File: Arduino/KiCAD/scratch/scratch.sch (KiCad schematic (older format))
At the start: 3 parts

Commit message: Worked on basic schematic
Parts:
- added R? (x5): 220, symbol Device:R_US
- added RV? (x2): Joystick, symbol Device:R_POT_Dual_Separate
- added SW? (x4): SW_Push, symbol Switch:SW_Push
- R?: value R_US -> 220
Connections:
- net +5V: now also A?.27 (+5V), R?.2, SW?.1, SW?.1, SW?.1, SW?.1
- net B1: now also A?.13 (D10)
- net GNDREF: now also A?.29 (GND), A?.4 (GND), R?.2, R?.2, R?.2, R?.2, RV?.3, RV?.4
- net B4: now reaches A?.10 (D7)
- net B4: now also R?.1, SW?.2
- net B3: now reaches A?.11 (D8)
- net B3: now also R?.1, SW?.2
- net B2: now reaches A?.12 (D9)
- net B2: now also R?.1, SW?.2
- net A1: now reaches A?.19 (A0)
- net A1: now also RV?.5
- net A2: now reaches A?.20 (A1)
- net A2: now also RV?.2
- net JB1: now reaches A?.6 (D3)
- net JB1: now also R?.1, SW?.2
- new net: R?.1, RV?.1, RV?.6
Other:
- moved on the sheet: R?, SW?

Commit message: book keeping
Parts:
- gave numbers to parts that had none: 13
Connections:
- net A1: now also RV1.2; no longer RV1.5
- net A2: now also RV1.5; no longer RV1.2
- net GNDREF: now also RV1.1, RV1.6; no longer RV1.3, RV1.4
- new net: R3.1, RV1.3, RV1.4
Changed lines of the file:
@@
 $EndDescr
 $Comp
-L MCU_Module:Arduino_Nano_v2.x A?
+L MCU_Module:Arduino_Nano_v2.x A1
 U 1 1 5EB70971
 P 3450 2700
-F 0 "A?" H 3450 1611 50  0000 C CNN
+F 0 "A1" H 3450 1611 50  0000 C CNN
 F 1 "Arduino_Nano_v2.x" H 3450 1520 50  0000 C CNN
 F 2 "Module:Arduino_Nano" H 3450 2700 50  0001 C CIN
@@
 $EndComp
 $Comp
-L Switch:SW_Push SW?
+L Switch:SW_Push SW1
 U 1 1 5EB728D4
 P 5850 1900
-F 0 "SW?" H 5850 2185 50  0000 C CNN
+F 0 "SW1" H 5850 2185 50  0000 C CNN
 F 1 "SW_Push" H 5850 2094 50  0000 C CNN
 F 2 "" H 5850 2100 50  0001 C CNN
@@
 $EndComp
 $Comp
-L Device:R_US R?
+L Device:R_US R1
 U 1 1 5EB73329
 P 6050 2150
-F 0 "R?" H 6118 2196 50  0000 L CNN
+F 0 "R1" H 6118 2196 50  0000 L CNN
 F 1 "220" H 6118 2105 50  0000 L CNN
 F 2 "" V 6090 2140 50  0001 C CNN
@@
 $EndComp
 $Comp
-L power:GNDREF #PWR?
+L power:GNDREF #PWR04
 U 1 1 5EB73B39
 P 6050 2350
-F 0 "#PWR?" H 6050 2100 50  0001 C CNN
+F 0 "#PWR04" H 6050 2100 50  0001 C CNN
 F 1 "GNDREF" H 6055 2177 50  0000 C CNN
 F 2 "" H 6050 2350 50  0001 C CNN
@@
 $EndComp
 $Comp
-L power:+5V #PWR?
+L power:+5V #PWR03
 U 1 1 5EB7405F
 P 5550 1700
-F 0 "#PWR?" H 5550 1550 50  0001 C CNN
+F 0 "#PWR03" H 5550 1550 50  0001 C CNN
 F 1 "+5V" H 5565 1873 50  0000 C CNN
 F 2 "" H 5550 1700 50  0001 C CNN
@@
 	6050 1950 6050 2000
 $Comp
-L Switch:SW_Push SW?
+L Switch:SW_Push SW2
 U 1 1 5EB7902D
 P 6850 1900
-F 0 "SW?" H 6850 2185 50  0000 C CNN
+F 0 "SW2" H 6850 2185 50  0000 C CNN
 F 1 "SW_Push" H 6850 2094 50  0000 C CNN
 F 2 "" H 6850 2100 50  0001 C CNN
@@
 $EndComp
 $Comp
-L Device:R_US R?
+L Device:R_US R2
 U 1 1 5EB79033
 P 7050 2150
-F 0 "R?" H 7118 2196 50  0000 L CNN
+F 0 "R2" H 7118 2196 50  0000 L CNN
 F 1 "220" H 7118 2105 50  0000 L CNN
 F 2 "" V 7090 2140 50  0001 C CNN
@@
 $EndComp
 $Comp
-L power:GNDREF #PWR?
+L power:GNDREF #PWR06
 U 1 1 5EB79039
 P 7050 2350
-F 0 "#PWR?" H 7050 2100 50  0001 C CNN
+F 0 "#PWR06" H 7050 2100 50  0001 C CNN
 F 1 "GNDREF" H 7055 2177 50  0000 C CNN
 F 2 "" H 7050 2350 50  0001 C CNN
@@
 $EndComp
 $Comp
-L power:+5V #PWR?
+L power:+5V #PWR05
 U 1 1 5EB7903F
 P 6550 1700
-F 0 "#PWR?" H 6550 1550 50  0001 C CNN
+F 0 "#PWR05" H 6550 1550 50  0001 C CNN
 F 1 "+5V" H 6565 1873 50  0000 C CNN
 F 2 "" H 6550 1700 50  0001 C CNN
@@
 	7050 1950 7050 2000
 $Comp
-L Switch:SW_Push SW?
+L Switch:SW_Push SW4
 U 1 1 5EB7CE6C
 P 7850 1900
-F 0 "SW?" H 7850 2185 50  0000 C CNN
+F 0 "SW4" H 7850 2185 50  0000 C CNN
 F 1 "SW_Push" H 7850 2094 50  0000 C CNN
 F 2 "" H 7850 2100 50  0001 C CNN
@@
 $EndComp
 $Comp
-L Device:R_US R?
+L Device:R_US R5
 U 1 1 5EB7CE72
 P 8050 2150
-F 0 "R?" H 8118 2196 50  0000 L CNN
+F 0 "R5" H 8118 2196 50  0000 L CNN
 F 1 "220" H 8118 2105 50  0000 L CNN
 F 2 "" V 8090 2140 50  0001 C CNN
@@
 $EndComp
 $Comp
-L power:GNDREF #PWR?
+L power:GNDREF #PWR011
 U 1 1 5EB7CE78
 P 8050 2350
-F 0 "#PWR?" H 8050 2100 50  0001 C CNN
+F 0 "#PWR011" H 8050 2100 50  0001 C CNN
 F 1 "GNDREF" H 8055 2177 50  0000 C CNN
 F 2 "" H 8050 2350 50  0001 C CNN
@@
 $EndComp
 $Comp
-L power:+5V #PWR?
+L power:+5V #PWR09
 U 1 1 5EB7CE7E
 P 7550 1700
-F 0 "#PWR?" H 7550 1550 50  0001 C CNN
+F 0 "#PWR09" H 7550 1550 50  0001 C CNN
 F 1 "+5V" H 7565 1873 50  0000 C CNN
 F 2 "" H 7550 1700 50  0001 C CNN
@@
 	8050 1950 8050 2000
 $Comp
-L Switch:SW_Push SW?
+L Switch:SW_Push SW5
 U 1 1 5EB7E073
 P 8850 1900
-F 0 "SW?" H 8850 2185 50  0000 C CNN
+F 0 "SW5" H 8850 2185 50  0000 C CNN
 F 1 "SW_Push" H 8850 2094 50  0000 C CNN
 F 2 "" H 8850 2100 50  0001 C CNN
@@
 $EndComp
 $Comp
-L Device:R_US R?
+L Device:R_US R6
 U 1 1 5EB7E079
 P 9050 2150
-F 0 "R?" H 9118 2196 50  0000 L CNN
+F 0 "R6" H 9118 2196 50  0000 L CNN
 F 1 "220" H 9118 2105 50  0000 L CNN
 F 2 "" V 9090 2140 50  0001 C CNN
@@
 $EndComp
 $Comp
-L power:GNDREF #PWR?
+L power:GNDREF #PWR013
 U 1 1 5EB7E07F
 P 9050 2350
-F 0 "#PWR?" H 9050 2100 50  0001 C CNN
+F 0 "#PWR013" H 9050 2100 50  0001 C CNN
 F 1 "GNDREF" H 9055 2177 50  0000 C CNN
 F 2 "" H 9050 2350 50  0001 C CNN
@@
 $EndComp
 $Comp
-L power:+5V #PWR?
+L power:+5V #PWR012
 U 1 1 5EB7E085
 P 8550 1700
-F 0 "#PWR?" H 8550 1550 50  0001 C CNN
+F 0 "#PWR012" H 8550 1550 50  0001 C CNN
 F 1 "+5V" H 8565 1873 50  0000 C CNN
 F 2 "" H 8550 1700 50  0001 C CNN
@@
 	2700 2800 2950 2800
 $Comp
-L power:GNDREF #PWR?
+L power:GNDREF #PWR02
 U 1 1 5EB79925
 P 4050 3700
-F 0 "#PWR?" H 4050 3450 50  0001 C CNN
+F 0 "#PWR02" H 4050 3450 50  0001 C CNN
 F 1 "GNDREF" H 4055 3527 50  0000 C CNN
 F 2 "" H 4050 3700 50  0001 C CNN
@@
 	3550 3700 4050 3700
 $Comp
-L power:+5V #PWR?
+L power:+5V #PWR01
 U 1 1 5EB7A78D
 P 3650 1500
-F 0 "#PWR?" H 3650 1350 50  0001 C CNN
+F 0 "#PWR01" H 3650 1350 50  0001 C CNN
 F 1 "+5V" H 3665 1673 50  0000 C CNN
 F 2 "" H 3650 1500 50  0001 C CNN
@@
 	3650 1500 3650 1700
 $Comp
-L Device:R_POT_Dual_Separate RV?
-U 1 1 5EB7B0B5
+L Device:R_POT_Dual_Separate RV1
+U 2 1 5EB7B0B5
 P 7550 4150
-F 0 "RV?" H 7480 4196 50  0000 R CNN
+F 0 "RV1" H 7480 4196 50  0000 R CNN
 F 1 "Joystick" H 7480 4105 50  0000 R CNN
 F 2 "" H 7550 4150 50  0001 C CNN
 F 3 "~" H 7550 4150 50  0001 C CNN
-	1    7550 4150
-	1    0    0    -1
-$EndComp
-$Comp
-L Device:R_POT_Dual_Separate RV?
-U 2 1 5EB7BB5A
+	2    7550 4150
+	1    0    0    -1
+$EndComp
+$Comp
+L Device:R_POT_Dual_Separate RV1
+U 1 1 5EB7BB5A
 P 7150 4450
-F 0 "RV?" H 7080 4404 50  0000 R CNN
+F 0 "RV1" H 7080 4404 50  0000 R CNN
 F 1 "Joystick" H 7080 4495 50  0000 R CNN
 F 2 "" H 7150 4450 50  0001 C CNN
 F 3 "~" H 7150 4450 50  0001 C CNN
-	2    7150 4450
+	1    7150 4450
 	-1   0    0    1
 $EndComp
 $Comp
-L Device:R_US R?
+L Device:R_US R3
 U 1 1 5EB7FD75
 P 7150 3850
-F 0 "R?" H 7218 3896 50  0000 L CNN
+F 0 "R3" H 7218 3896 50  0000 L CNN
 F 1 "220" H 7218 3805 50  0000 L CNN
 F 2 "" V 7190 3840 50  0001 C CNN
@@
 	7550 3900 7550 4000
 $Comp
-L power:+5V #PWR?
+L power:+5V #PWR07
 U 1 1 5EB81F8A
 P 7150 3650
-F 0 "#PWR?" H 7150 3500 50  0001 C CNN
+F 0 "#PWR07" H 7150 3500 50  0001 C CNN
 F 1 "+5V" H 7165 3823 50  0000 C CNN
 F 2 "" H 7150 3650 50  0001 C CNN
@@
 $EndComp
 $Comp
-L power:GNDREF #PWR?
+L power:GNDREF #PWR08
 U 1 1 5EB83127
 P 7400 4950
-F 0 "#PWR?" H 7400 4700 50  0001 C CNN
+F 0 "#PWR08" H 7400 4700 50  0001 C CNN
 F 1 "GNDREF" H 7405 4777 50  0000 C CNN
 F 2 "" H 7400 4950 50  0001 C CNN
@@
 	7150 4050 7150 4300
 $Comp
-L Switch:SW_Push SW?
+L Switch:SW_Push SW3
 U 1 1 5EB8C018
 P 7800 4100
-F 0 "SW?" H 7800 4385 50  0000 C CNN
+F 0 "SW3" H 7800 4385 50  0000 C CNN
 F 1 "SW_Push" H 7800 4294 50  0000 C CNN
 F 2 "" H 7800 4300 50  0001 C CNN
@@
 $EndComp
 $Comp
-L power:+5V #PWR?
+L power:+5V #PWR010
 U 1 1 5EB8C02A
 P 7800 3850
-F 0 "#PWR?" H 7800 3700 50  0001 C CNN
+F 0 "#PWR010" H 7800 3700 50  0001 C CNN
 F 1 "+5V" H 7815 4023 50  0000 C CNN
 F 2 "" H 7800 3850 50  0001 C CNN
@@
 	7800 4400 7800 4450
 $Comp
-L Device:R_US R?
+L Device:R_US R4
 U 1 1 5EB8C01E
 P 7800 4600
-F 0 "R?" H 7868 4646 50  0000 L CNN
+F 0 "R4" H 7868 4646 50  0000 L CNN
 F 1 "220" H 7868 4555 50  0000 L CNN
 F 2 "" V 7840 4590 50  0001 C CNN

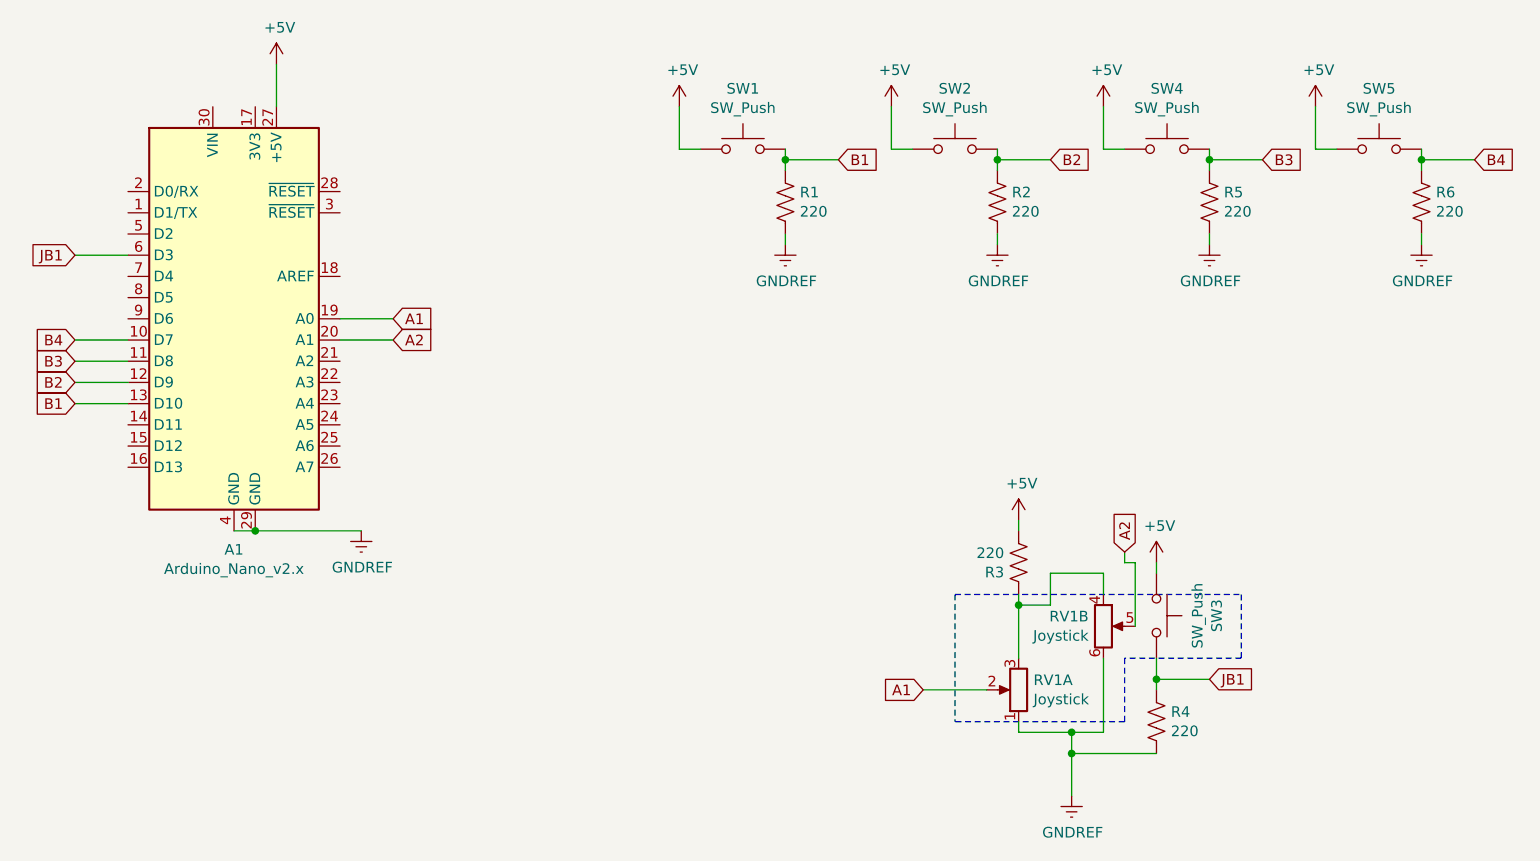
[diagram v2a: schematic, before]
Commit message: Added a scratch pad for arduino software. Addressed a potential problem in schematic.
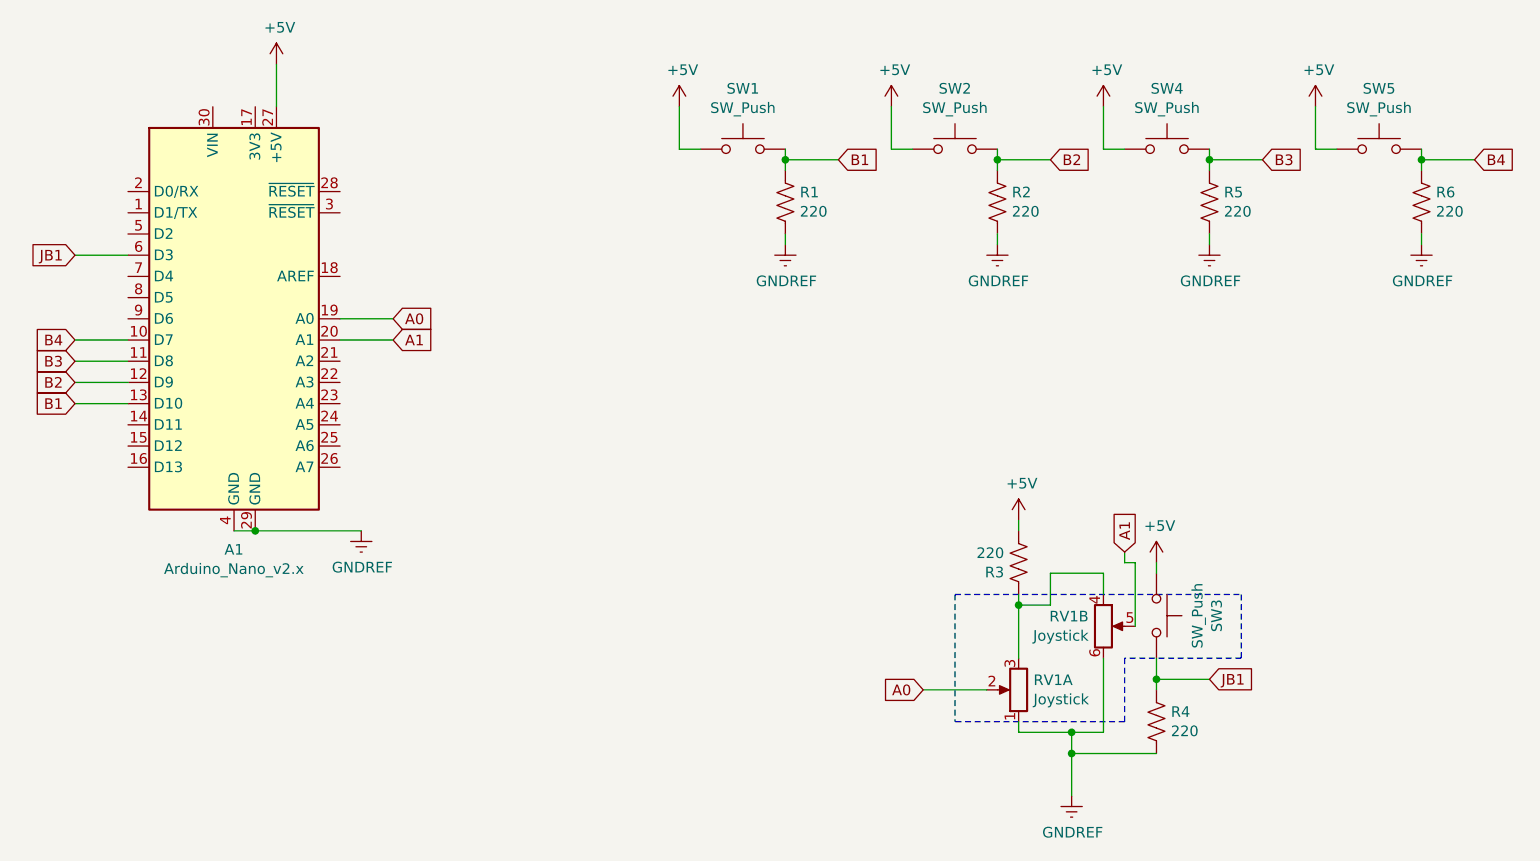
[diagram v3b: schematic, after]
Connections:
- net A2 is gone; now on net A1: A1.20 (A1), RV1.5
- net A1: no longer A1.19 (A0), RV1.2
- new net A0: A1.19 (A0), RV1.2
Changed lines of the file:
@@
 	6850 4000 6850 4600
 Text GLabel 6700 4450 0    50   Input ~ 0
+A0
+Text GLabel 7650 3800 1    50   Input ~ 0
 A1
-Text GLabel 7650 3800 1    50   Input ~ 0
-A2
 Text GLabel 8050 4400 2    50   Input ~ 0
 JB1
@@
 	7650 3850 7650 3800
 Text GLabel 4200 2700 2    50   Input ~ 0
-A1
+A0
 Wire Wire Line
 	4200 2700 3950 2700
 Text GLabel 4200 2800 2    50   Input ~ 0
-A2
+A1
 Wire Wire Line
 	4200 2800 3950 2800

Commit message: TODO button and joystick footprint design
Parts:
- R1, R2, R3, R4, R5, R6: footprint (none) -> LED_SMD:LED_0805_2012Metric_Pad1.15x1.40mm_HandSolder
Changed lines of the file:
@@
 F 0 "R1" H 6118 2196 50  0000 L CNN
 F 1 "220" H 6118 2105 50  0000 L CNN
-F 2 "" V 6090 2140 50  0001 C CNN
+F 2 "LED_SMD:LED_0805_2012Metric_Pad1.15x1.40mm_HandSolder" V 6090 2140 50  0001 C CNN
 F 3 "~" H 6050 2150 50  0001 C CNN
 	1    6050 2150
@@
 F 0 "R2" H 7118 2196 50  0000 L CNN
 F 1 "220" H 7118 2105 50  0000 L CNN
-F 2 "" V 7090 2140 50  0001 C CNN
+F 2 "LED_SMD:LED_0805_2012Metric_Pad1.15x1.40mm_HandSolder" V 7090 2140 50  0001 C CNN
 F 3 "~" H 7050 2150 50  0001 C CNN
 	1    7050 2150
@@
 F 0 "R5" H 8118 2196 50  0000 L CNN
 F 1 "220" H 8118 2105 50  0000 L CNN
-F 2 "" V 8090 2140 50  0001 C CNN
+F 2 "LED_SMD:LED_0805_2012Metric_Pad1.15x1.40mm_HandSolder" V 8090 2140 50  0001 C CNN
 F 3 "~" H 8050 2150 50  0001 C CNN
 	1    8050 2150
@@
 F 0 "R6" H 9118 2196 50  0000 L CNN
 F 1 "220" H 9118 2105 50  0000 L CNN
-F 2 "" V 9090 2140 50  0001 C CNN
+F 2 "LED_SMD:LED_0805_2012Metric_Pad1.15x1.40mm_HandSolder" V 9090 2140 50  0001 C CNN
 F 3 "~" H 9050 2150 50  0001 C CNN
 	1    9050 2150
@@
 F 0 "R3" H 7218 3896 50  0000 L CNN
 F 1 "220" H 7218 3805 50  0000 L CNN
-F 2 "" V 7190 3840 50  0001 C CNN
+F 2 "LED_SMD:LED_0805_2012Metric_Pad1.15x1.40mm_HandSolder" V 7190 3840 50  0001 C CNN
 F 3 "~" H 7150 3850 50  0001 C CNN
 	1    7150 3850
@@
 F 0 "R4" H 7868 4646 50  0000 L CNN
 F 1 "220" H 7868 4555 50  0000 L CNN
-F 2 "" V 7840 4590 50  0001 C CNN
+F 2 "LED_SMD:LED_0805_2012Metric_Pad1.15x1.40mm_HandSolder" V 7840 4590 50  0001 C CNN
 F 3 "~" H 7800 4600 50  0001 C CNN
 	1    7800 4600
